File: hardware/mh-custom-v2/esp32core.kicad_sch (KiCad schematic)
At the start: 1 part, among them U1 ESP32-DEVKITC-32D

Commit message: laptop back, coordinating efforts
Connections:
- net ade7953-IRQ: now also U1.9 (IO25); no longer U1.12 (IO14)
- net ade7953-reset: now also U1.12 (IO14); no longer U1.29 (IO5)
- net buzz: now also U1.29 (IO5); no longer U1.9 (IO25)
- net +3V3 renamed +3.3V
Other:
- note removed: "fixed-in-place"

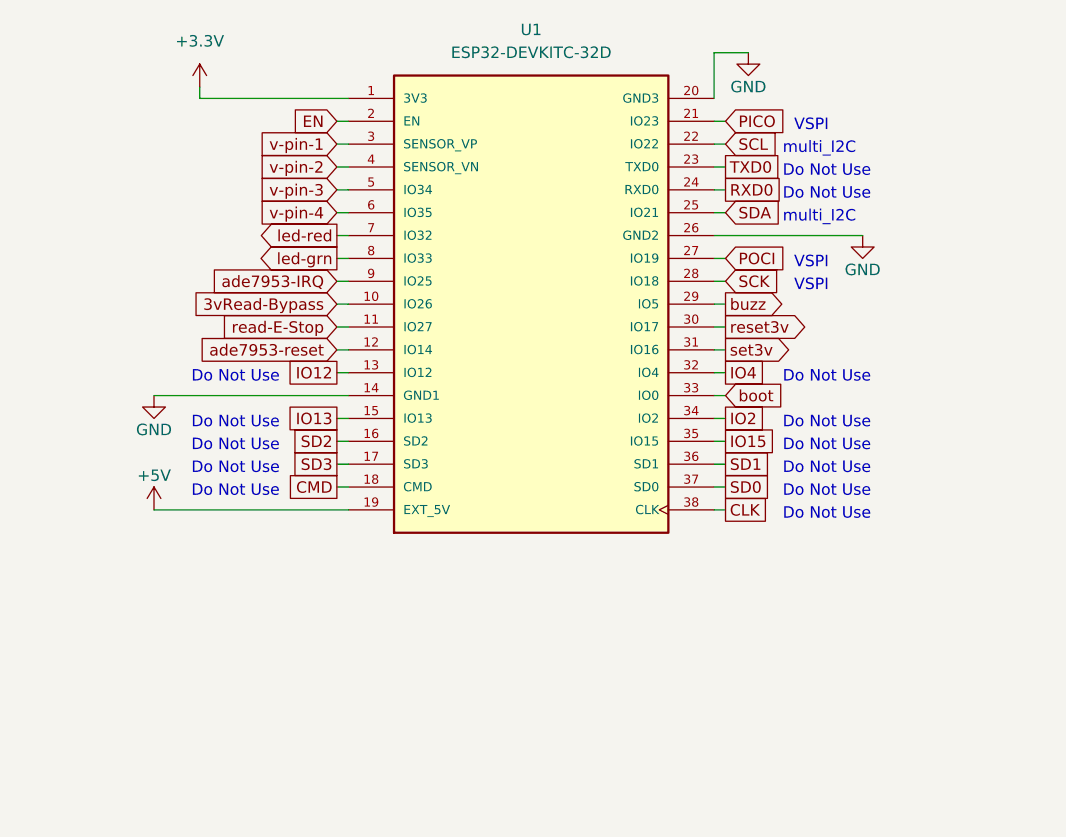
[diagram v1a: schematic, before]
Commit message: added linear regulator for 3.3V peripherals and ADE7953 reset jumper
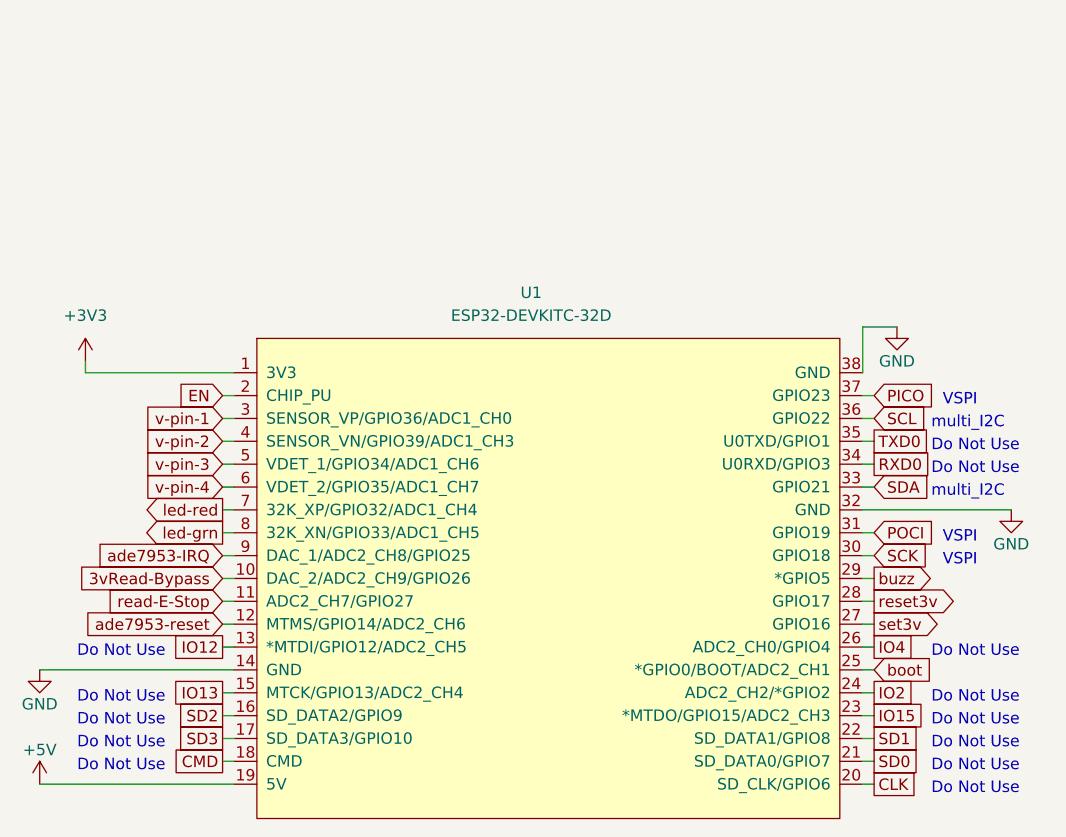
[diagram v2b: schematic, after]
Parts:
- U1: footprint esp32-devkitc-v4:MODULE_ESP32-DEVKITC-32D -> Espressif:ESP32-DevKitC; symbol esp32-devkitc-v4:ESP32-DEVKITC-32D -> espressif:ESP32-DevKitC; now in the parts list
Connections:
- net CLK: now also U1.20 (SD_CLK/GPIO6); no longer U1.38 (CLK)
- net GND: now also U1.32 (GND), U1.38 (GND); no longer U1.20 (GND3), U1.26 (GND2)
- net IO15: now also U1.23 (*MTDO/GPIO15/ADC2_CH3); no longer U1.35 (IO15)
- net IO2: now also U1.24 (ADC2_CH2/*GPIO2); no longer U1.34 (IO2)
- net IO4: now also U1.26 (ADC2_CH0/GPIO4); no longer U1.32 (IO4)
- net PICO: now also U1.37 (GPIO23); no longer U1.21 (IO23)
- net POCI: now also U1.31 (GPIO19); no longer U1.27 (IO19)
- net RXD0: now also U1.34 (U0RXD/GPIO3); no longer U1.24 (RXD0)
- net SCK: now also U1.30 (GPIO18); no longer U1.28 (IO18)
- net SCL: now also U1.36 (GPIO22); no longer U1.22 (IO22)
- net SD0: now also U1.21 (SD_DATA0/GPIO7); no longer U1.37 (SD0)
- net SD1: now also U1.22 (SD_DATA1/GPIO8); no longer U1.36 (SD1)
- net SDA: now also U1.33 (GPIO21); no longer U1.25 (IO21)
- net TXD0: now also U1.35 (U0TXD/GPIO1); no longer U1.23 (TXD0)
- net boot: now also U1.25 (*GPIO0/BOOT/ADC2_CH1); no longer U1.33 (IO0)
- net reset3v: now also U1.28 (GPIO17); no longer U1.30 (IO17)
- net set3v: now also U1.27 (GPIO16); no longer U1.31 (IO16)
- net +3.3V renamed +3V3
